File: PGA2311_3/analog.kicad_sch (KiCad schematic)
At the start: 88 parts, among them J201 3, J202 3, J203 2, J204 2, U201 OPA1678IDR, U202 CD74HCT4052, U203 CD74HCT4052, U204 LM337LM, U205 PGA2311UA, U206 LM317LIDR, U207 UA78L05AIDR

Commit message: Add files via upload
CS3 line added to connector
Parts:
- removed R229: 0, Resistor_SMD:R_0805_2012Metric_Pad1.20x1.40mm_HandSolder, symbol Device:R_Small
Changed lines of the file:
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@@
 		(title "Preamp2311")
 		(date "03.2026")
-		(rev "2")
+		(rev "2_1")
 		(company "DMSDL")
 		(comment 1 "designed by Oleg Voitovich")
@@
 	(wire
 		(pts
-			(xy 205.74 69.85) (xy 205.74 73.66)
-		)
-		(stroke
-			(width 0)
-			(type default)
-		)
-	)
-	(wire
-		(pts
 			(xy 204.47 54.61) (xy 205.74 54.61)
 		)
@@
 	(wire
 		(pts
-			(xy 205.74 69.85) (xy 208.28 69.85)
-		)
-		(stroke
-			(width 0)
-			(type default)
-		)
-	)
-	(wire
-		(pts
 			(xy 110.49 142.24) (xy 113.03 142.24)
 		)
@@
 	(wire
 		(pts
-			(xy 213.36 69.85) (xy 214.63 69.85)
-		)
-		(stroke
-			(width 0)
-			(type default)
-		)
-	)
-	(wire
-		(pts
 			(xy 142.24 180.34) (xy 142.24 181.61)
 		)
@@
 	(wire
 		(pts
-			(xy 214.63 69.85) (xy 214.63 73.66)
-		)
-		(stroke
-			(width 0)
-			(type default)
-		)
-	)
-	(wire
-		(pts
 			(xy 223.52 142.24) (xy 226.06 142.24)
 		)
@@
 	(symbol
 		(lib_id "power:GND")
-		(at 205.74 73.66 0)
-		(unit 1)
-		(exclude_from_sim no)
-		(in_bom yes)
-		(on_board yes)
-		(dnp no)
-		(property "Reference" "#PWR0249"
-			(at 205.74 80.01 0)
-			(effects
-				(font
-					(size 1.27 1.27)
-				)
-				(hide yes)
-			)
-		)
-		(property "Value" "GND"
-			(at 210.058 75.692 0)
-			(effects
-				(font
-					(size 1.27 1.27)
-				)
-			)
-		)
-		(property "Footprint" ""
-			(at 205.74 73.66 0)
-			(effects
-				(font
-					(size 1.27 1.27)
-				)
-				(hide yes)
-			)
-		)
-		(property "Datasheet" ""
-			(at 205.74 73.66 0)
-			(effects
-				(font
-					(size 1.27 1.27)
-				)
-				(hide yes)
-			)
-		)
-		(property "Description" "Power symbol creates a global label with name \"GND\" , ground"
-			(at 205.74 73.66 0)
-			(effects
-				(font
-					(size 1.27 1.27)
-				)
-				(hide yes)
-			)
-		)
-		(pin "1"
-		)
-		(instances
-			(project "PGA2311_3"
-				(path "/e4f5d1ca-8b46-4ca2-bb25-7f237c56d603/417e42a4-c07c-47f8-ba75-79030ad924cb"
-					(reference "#PWR0249")
-					(unit 1)
-				)
-			)
-		)
-	)
-	(symbol
-		(lib_id "power:GND")
 		(at 134.62 64.77 0)
 		(unit 1)
@@
 	)
 	(symbol
-		(lib_id "Device:R_Small")
-		(at 210.82 69.85 270)
-		(unit 1)
-		(exclude_from_sim no)
-		(in_bom yes)
-		(on_board yes)
-		(dnp no)
-		(property "Reference" "R229"
-			(at 214.63 66.802 90)
-			(effects
-				(font
-					(size 1.016 1.016)
-				)
-			)
-		)
-		(property "Value" "0"
-			(at 209.55 67.056 90)
-			(effects
-				(font
-					(size 1.27 1.27)
-				)
-			)
-		)
-		(property "Footprint" "Resistor_SMD:R_0805_2012Metric_Pad1.20x1.40mm_HandSolder"
-			(at 210.82 69.85 0)
-			(effects
-				(font
-					(size 1.27 1.27)
-				)
-				(hide yes)
-			)
-		)
-		(property "Datasheet" "~"
-			(at 210.82 69.85 0)
-			(effects
-				(font
-					(size 1.27 1.27)
-				)
-				(hide yes)
-			)
-		)
-		(property "Description" "Resistor, small symbol"
-			(at 210.82 69.85 0)
-			(effects
-				(font
-					(size 1.27 1.27)
-				)
-				(hide yes)
-			)
-		)
-		(pin "1"
-		)
-		(pin "2"
-		)
-		(instances
-			(project "PGA2311_3"
-				(path "/e4f5d1ca-8b46-4ca2-bb25-7f237c56d603/417e42a4-c07c-47f8-ba75-79030ad924cb"
-					(reference "R229")
-					(unit 1)
-				)
-			)
-		)
-	)
-	(symbol
 		(lib_id "power:GND")
 		(at 134.62 90.17 0)
@@
 					(unit 1)
 				)
-			)
-		)
-	)
-	(symbol
-		(lib_id "power:GND")
-		(at 214.63 73.66 0)
-		(unit 1)
-		(exclude_from_sim no)
-		(in_bom yes)
-		(on_board yes)
-		(dnp no)
-		(property "Reference" "#PWR0250"
-			(at 214.63 80.01 0)
-			(effects
-				(font
-					(size 1.27 1.27)
-				)
-				(hide yes)
-			)
-		)
-		(property "Value" "GND"
-			(at 218.948 75.692 0)
-			(effects
-				(font
-					(size 1.27 1.27)
-				)
-			)
-		)
-		(property "Footprint" ""
-			(at 214.63 73.66 0)
-			(effects
-				(font
-					(size 1.27 1.27)
-				)
-				(hide yes)
-			)
-		)
-		(property "Datasheet" ""
-			(at 214.63 73.66 0)
-			(effects
-				(font
-					(size 1.27 1.27)
-				)
-				(hide yes)
-			)
-		)
-		(property "Description" "Power symbol creates a global label with name \"GND\" , ground"
-			(at 214.63 73.66 0)
-			(effects
-				(font
-					(size 1.27 1.27)
-				)
-				(hide yes)
-			)
-		)
-		(pin "1"
-		)
-		(instances
-			(project "PGA2311_3"
-				(path "/e4f5d1ca-8b46-4ca2-bb25-7f237c56d603/417e42a4-c07c-47f8-ba75-79030ad924cb"
-					(reference "#PWR0250")
-					(unit 1)
-				)

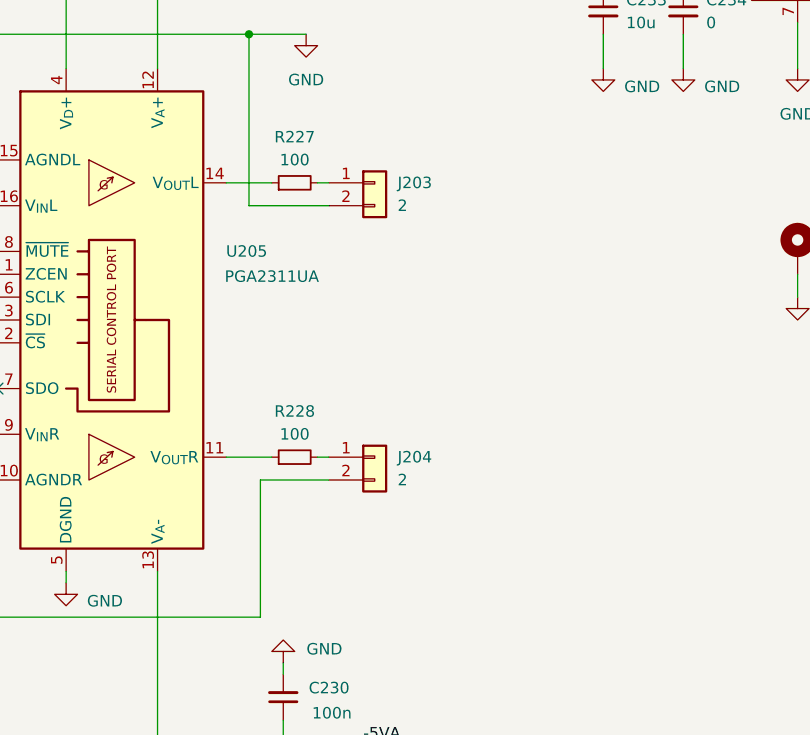
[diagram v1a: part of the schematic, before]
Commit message: Add files via upload
PGA output connector added
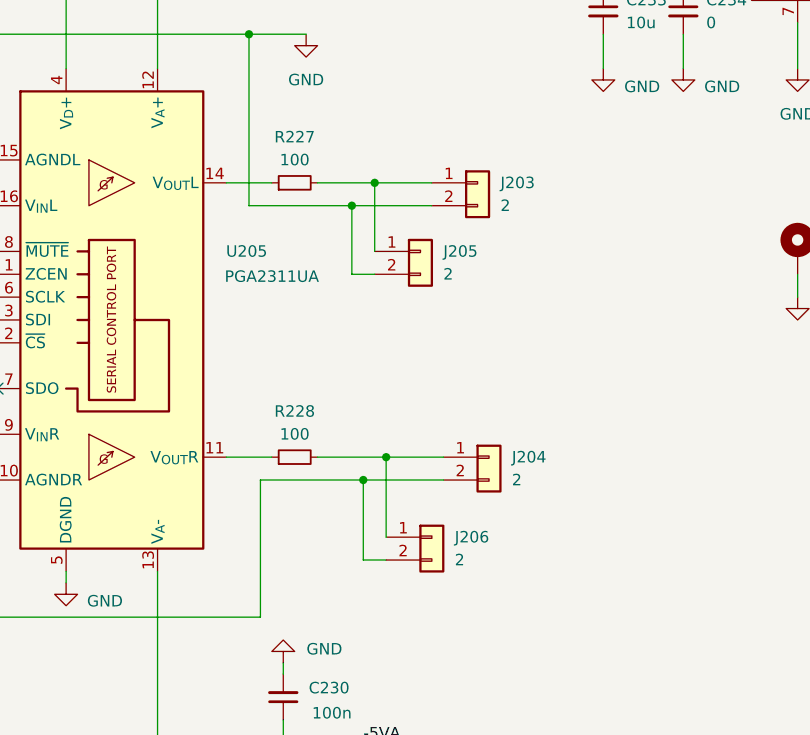
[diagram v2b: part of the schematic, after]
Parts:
- added J205, J206: 2, Connector_PinHeader_2.54mm:PinHeader_1x02_P2.54mm_Vertical, symbol Connector_Generic:Conn_01x02
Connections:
- net GND: now also J205.2 (Pin_2), J206.2 (Pin_2)
- net at J204.1 (Pin_1), R228.2: now also J206.1 (Pin_1)
- net at J203.1 (Pin_1), R227.2: now also J205.1 (Pin_1)
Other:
- moved on the sheet: J203, J204

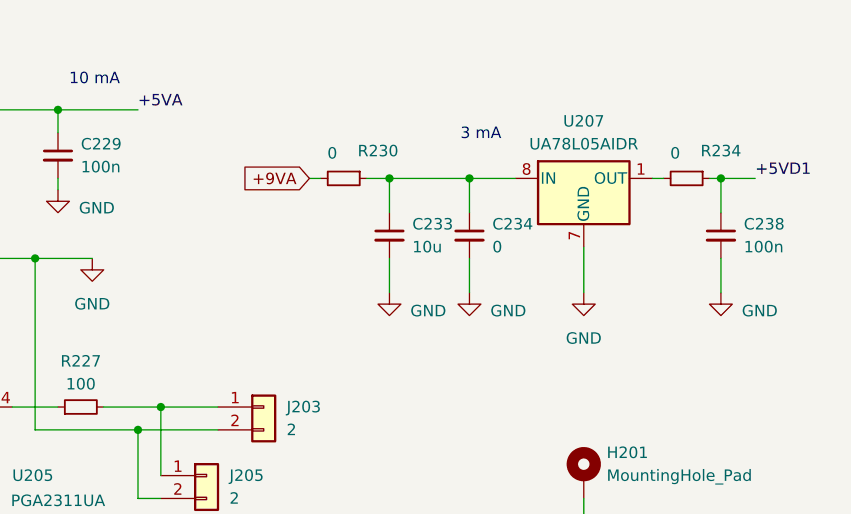
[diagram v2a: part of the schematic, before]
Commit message: Add files via upload
vias rearranged for connector placement
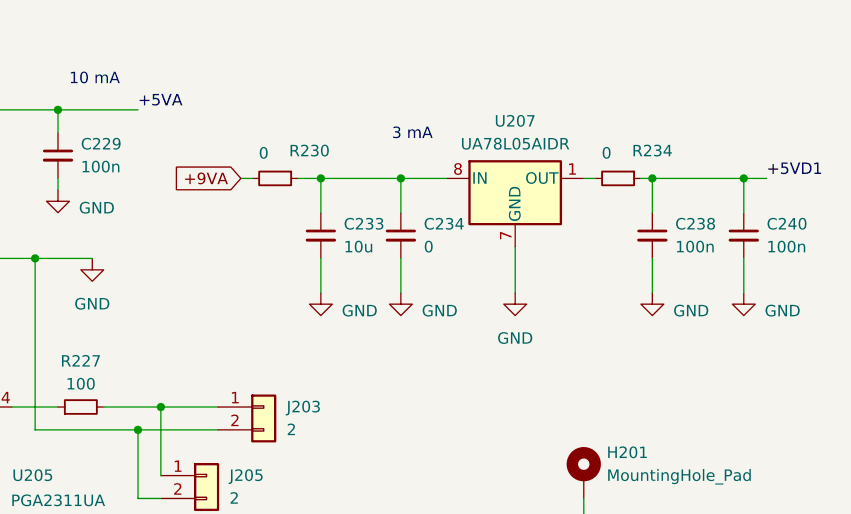
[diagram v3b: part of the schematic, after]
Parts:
- added C240: 100n, Capacitor_SMD:C_0805_2012Metric_Pad1.18x1.45mm_HandSolder, symbol Device:C_Small
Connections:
- net +5VD1: now also C240.1
- net GND: now also C240.2
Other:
- moved on the sheet: C233, C234, C238, R230, R234, U207

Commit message: Add files via upload
v.2.4 connector to +VA line added
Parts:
- added J207: 2, Connector_PinHeader_2.54mm:PinHeader_1x02_P2.54mm_Vertical, symbol Connector_Generic:Conn_01x02
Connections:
- net +9VA: now also J207.2 (Pin_2)
- net GND: now also J207.1 (Pin_1)
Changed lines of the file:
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@@
 		(title "Preamp2311")
 		(date "03.2026")
-		(rev "2_3")
+		(rev "2_4")
 		(company "DMSDL")
 		(comment 1 "designed by Oleg Voitovich")
@@
 	)
 	(junction
+		(at 180.34 142.24)
+		(diameter 0)
+		(color 0 0 0 0)
+	)
+	(junction
 		(at 132.08 172.72)
 		(diameter 0)
@@
 	(wire
 		(pts
-			(xy 184.15 142.24) (xy 185.42 142.24)
+			(xy 173.99 142.24) (xy 180.34 142.24)
 		)
 		(stroke
@@
 	(wire
 		(pts
+			(xy 180.34 142.24) (xy 185.42 142.24)
+		)
+		(stroke
+			(width 0)
+			(type default)
+		)
+	)
+	(wire
+		(pts
 			(xy 172.72 16.51) (xy 190.5 16.51)
 		)
@@
 	(wire
 		(pts
+			(xy 181.61 133.35) (xy 180.34 133.35)
+		)
+		(stroke
+			(width 0)
+			(type default)
+		)
+	)
+	(wire
+		(pts
 			(xy 26.67 58.42) (xy 26.67 66.04)
 		)
@@
 	(wire
 		(pts
+			(xy 173.99 130.81) (xy 181.61 130.81)
+		)
+		(stroke
+			(width 0)
+			(type default)
+		)
+	)
+	(wire
+		(pts
 			(xy 97.79 66.04) (xy 96.52 66.04)
 		)
@@
 	(wire
 		(pts
+			(xy 173.99 130.81) (xy 173.99 134.62)
+		)
+		(stroke
+			(width 0)
+			(type default)
+		)
+	)
+	(wire
+		(pts
 			(xy 30.48 39.37) (xy 30.48 43.18)
 		)
@@
 	(wire
 		(pts
+			(xy 180.34 133.35) (xy 180.34 142.24)
+		)
+		(stroke
+			(width 0)
+			(type default)
+		)
+	)
+	(wire
+		(pts
 			(xy 124.46 81.28) (xy 124.46 72.39)
 		)
@@
 	(global_label "+9VA"
 		(shape input)
-		(at 184.15 142.24 180)
+		(at 173.99 142.24 180)
 		(fields_autoplaced yes)
 		(effects
@@
 		)
 		(property "Intersheetrefs" "${INTERSHEET_REFS}"
-			(at 176.2057 142.24 0)
+			(at 166.0457 142.24 0)
 			(effects
 				(font
@@
 	(symbol
 		(lib_id "power:GND")
+		(at 173.99 134.62 0)
+		(unit 1)
+		(exclude_from_sim no)
+		(in_bom yes)
+		(on_board yes)
+		(dnp no)
+		(property "Reference" "#PWR0250"
+			(at 173.99 140.97 0)
+			(effects
+				(font
+					(size 1.27 1.27)
+				)
+				(hide yes)
+			)
+		)
+		(property "Value" "GND"
+			(at 178.308 136.652 0)
+			(effects
+				(font
+					(size 1.27 1.27)
+				)
+			)
+		)
+		(property "Footprint" ""
+			(at 173.99 134.62 0)
+			(effects
+				(font
+					(size 1.27 1.27)
+				)
+				(hide yes)
+			)
+		)
+		(property "Datasheet" ""
+			(at 173.99 134.62 0)
+			(effects
+				(font
+					(size 1.27 1.27)
+				)
+				(hide yes)
+			)
+		)
+		(property "Description" "Power symbol creates a global label with name \"GND\" , ground"
+			(at 173.99 134.62 0)
+			(effects
+				(font
+					(size 1.27 1.27)
+				)
+				(hide yes)
+			)
+		)
+		(pin "1"
+		)
+		(instances
+			(project "PGA2311_3"
+				(path "/e4f5d1ca-8b46-4ca2-bb25-7f237c56d603/417e42a4-c07c-47f8-ba75-79030ad924cb"
+					(reference "#PWR0250")
+					(unit 1)
+				)
+			)
+		)
+	)
+	(symbol
+		(lib_id "power:GND")
 		(at 203.2 38.1 0)
 		(unit 1)
@@
 					(unit 1)
 				)
+			)
+		)
+	)
+	(symbol
+		(lib_id "Connector_Generic:Conn_01x02")
+		(at 186.69 130.81 0)
+		(unit 1)
+		(exclude_from_sim no)
+		(in_bom yes)
+		(on_board yes)
+		(dnp no)
+		(fields_autoplaced yes)
+		(property "Reference" "J207"
+			(at 189.23 130.8099 0)
+			(effects
+				(font
+					(size 1.27 1.27)
+				)
+				(justify left)
+			)
+		)
+		(property "Value" "2"
+			(at 189.23 133.3499 0)
+			(effects
+				(font
+					(size 1.27 1.27)
+				)
+				(justify left)
+			)
+		)
+		(property "Footprint" "Connector_PinHeader_2.54mm:PinHeader_1x02_P2.54mm_Vertical"
+			(at 186.69 130.81 0)
+			(effects
+				(font
+					(size 1.27 1.27)
+				)
+				(hide yes)
+			)
+		)
+		(property "Datasheet" "~"
+			(at 186.69 130.81 0)
+			(effects
+				(font
+					(size 1.27 1.27)
+				)
+				(hide yes)
+			)
+		)
+		(property "Description" "Generic connector, single row, 01x02, script generated (kicad-library-utils/schlib/autogen/connector/)"
+			(at 186.69 130.81 0)
+			(effects
+				(font
+					(size 1.27 1.27)
+				)
+				(hide yes)
+			)
+		)
+		(pin "1"
+		)
+		(pin "2"
+		)
+		(instances
+			(project "PGA2311_3"
+				(path "/e4f5d1ca-8b46-4ca2-bb25-7f237c56d603/417e42a4-c07c-47f8-ba75-79030ad924cb"
+					(reference "J207")
+					(unit 1)
+				)

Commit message: Add files via upload
78l05 output R0 removed
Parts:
- removed R234: 0, Resistor_SMD:R_0805_2012Metric_Pad1.20x1.40mm_HandSolder, symbol Device:R_Small
- R205, R206: value 10 -> 100
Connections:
- net +5VD1: now also U207.1 (OUT)
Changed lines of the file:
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@@
 	(wire
 		(pts
-			(xy 257.81 29.21) (xy 259.08 29.21)
+			(xy 257.81 29.21) (xy 265.43 29.21)
 		)
 		(stroke
@@
 	(wire
 		(pts
-			(xy 264.16 29.21) (xy 265.43 29.21)
-		)
-		(stroke
-			(width 0)
-			(type default)
-		)
-	)
-	(wire
-		(pts
 			(xy 163.83 64.77) (xy 163.83 34.29)
 		)
@@
 			)
 		)
-		(property "Value" "10"
+		(property "Value" "100"
 			(at 77.216 93.98 90)
 			(effects
@@
 			)
 		)
-		(property "Value" "10"
+		(property "Value" "100"
 			(at 74.676 15.24 90)
 			(effects
@@
 					(unit 1)
 				)
-			)
-		)
-	)
-	(symbol
-		(lib_id "Device:R_Small")
-		(at 261.62 29.21 270)
-		(unit 1)
-		(exclude_from_sim no)
-		(in_bom yes)
-		(on_board yes)
-		(dnp no)
-		(property "Reference" "R234"
-			(at 265.43 26.162 90)
-			(effects
-				(font
-					(size 1.27 1.27)
-				)
-			)
-		)
-		(property "Value" "0"
-			(at 260.35 26.416 90)
-			(effects
-				(font
-					(size 1.27 1.27)
-				)
-			)
-		)
-		(property "Footprint" "Resistor_SMD:R_0805_2012Metric_Pad1.20x1.40mm_HandSolder"
-			(at 261.62 29.21 0)
-			(effects
-				(font
-					(size 1.27 1.27)
-				)
-				(hide yes)
-			)
-		)
-		(property "Datasheet" "~"
-			(at 261.62 29.21 0)
-			(effects
-				(font
-					(size 1.27 1.27)
-				)
-				(hide yes)
-			)
-		)
-		(property "Description" "Resistor, small symbol"
-			(at 261.62 29.21 0)
-			(effects
-				(font
-					(size 1.27 1.27)
-				)
-				(hide yes)
-			)
-		)
-		(pin "1"
-		)
-		(pin "2"
-		)
-		(instances
-			(project "PGA2311_3"
-				(path "/e4f5d1ca-8b46-4ca2-bb25-7f237c56d603/417e42a4-c07c-47f8-ba75-79030ad924cb"
-					(reference "R234")
-					(unit 1)
-				)

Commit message: Add files via upload
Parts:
- C240: value 100n -> 10u
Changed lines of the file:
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@@
 			)
 		)
-		(property "Value" "100n"
+		(property "Value" "10u"
 			(at 278.13 36.8362 0)
 			(effects

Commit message: Add files via upload
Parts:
- added J208: 2, Connector_PinHeader_2.54mm:PinHeader_1x02_P2.54mm_Vertical, symbol Connector_Generic:Conn_01x02
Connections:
- net -9VA: now also J208.2 (Pin_2)
- net GND: now also J208.1 (Pin_1)
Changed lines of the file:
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@@
 	(wire
 		(pts
-			(xy 76.2 172.72) (xy 77.47 172.72)
+			(xy 71.12 172.72) (xy 77.47 172.72)
 		)
 		(stroke
@@
 	(wire
 		(pts
+			(xy 77.47 161.29) (xy 71.12 161.29)
+		)
+		(stroke
+			(width 0)
+			(type default)
+		)
+	)
+	(wire
+		(pts
 			(xy 161.29 34.29) (xy 161.29 62.23)
 		)
@@
 	(wire
 		(pts
+			(xy 71.12 161.29) (xy 71.12 166.37)
+		)
+		(stroke
+			(width 0)
+			(type default)
+		)
+	)
+	(wire
+		(pts
 			(xy 64.77 63.5) (xy 64.77 43.18)
 		)
@@
 	(wire
 		(pts
+			(xy 77.47 163.83) (xy 77.47 172.72)
+		)
+		(stroke
+			(width 0)
+			(type default)
+		)
+	)
+	(wire
+		(pts
 			(xy 162.56 172.72) (xy 162.56 175.26)
 		)
@@
 	(global_label "-9VA"
 		(shape input)
-		(at 76.2 172.72 180)
+		(at 71.12 172.72 180)
 		(fields_autoplaced yes)
 		(effects
@@
 		)
 		(property "Intersheetrefs" "${INTERSHEET_REFS}"
-			(at 68.2557 172.72 0)
+			(at 63.1757 172.72 0)
 			(effects
 				(font
@@
 	)
 	(symbol
+		(lib_id "Connector_Generic:Conn_01x02")
+		(at 82.55 161.29 0)
+		(unit 1)
+		(exclude_from_sim no)
+		(in_bom yes)
+		(on_board yes)
+		(dnp no)
+		(fields_autoplaced yes)
+		(property "Reference" "J208"
+			(at 85.09 161.2899 0)
+			(effects
+				(font
+					(size 1.27 1.27)
+				)
+				(justify left)
+			)
+		)
+		(property "Value" "2"
+			(at 85.09 163.8299 0)
+			(effects
+				(font
+					(size 1.27 1.27)
+				)
+				(justify left)
+			)
+		)
+		(property "Footprint" "Connector_PinHeader_2.54mm:PinHeader_1x02_P2.54mm_Vertical"
+			(at 82.55 161.29 0)
+			(effects
+				(font
+					(size 1.27 1.27)
+				)
+				(hide yes)
+			)
+		)
+		(property "Datasheet" "~"
+			(at 82.55 161.29 0)
+			(effects
+				(font
+					(size 1.27 1.27)
+				)
+				(hide yes)
+			)
+		)
+		(property "Description" "Generic connector, single row, 01x02, script generated (kicad-library-utils/schlib/autogen/connector/)"
+			(at 82.55 161.29 0)
+			(effects
+				(font
+					(size 1.27 1.27)
+				)
+				(hide yes)
+			)
+		)
+		(pin "1"
+		)
+		(pin "2"
+		)
+		(instances
+			(project "PGA2311_3"
+				(path "/e4f5d1ca-8b46-4ca2-bb25-7f237c56d603/417e42a4-c07c-47f8-ba75-79030ad924cb"
+					(reference "J208")
+					(unit 1)
+				)
+			)
+		)
+	)
+	(symbol
 		(lib_id "Device:C_Small")
 		(at 36.83 66.04 90)
@@
 					(unit 1)
 				)
+			)
+		)
+	)
+	(symbol
+		(lib_id "power:GND")
+		(at 71.12 166.37 0)
+		(unit 1)
+		(exclude_from_sim no)
+		(in_bom yes)
+		(on_board yes)
+		(dnp no)
+		(property "Reference" "#PWR0262"
+			(at 71.12 172.72 0)
+			(effects
+				(font
+					(size 1.27 1.27)
+				)
+				(hide yes)
+			)
+		)
+		(property "Value" "GND"
+			(at 75.438 168.402 0)
+			(effects
+				(font
+					(size 1.27 1.27)
+				)
+			)
+		)
+		(property "Footprint" ""
+			(at 71.12 166.37 0)
+			(effects
+				(font
+					(size 1.27 1.27)
+				)
+				(hide yes)
+			)
+		)
+		(property "Datasheet" ""
+			(at 71.12 166.37 0)
+			(effects
+				(font
+					(size 1.27 1.27)
+				)
+				(hide yes)
+			)
+		)
+		(property "Description" "Power symbol creates a global label with name \"GND\" , ground"
+			(at 71.12 166.37 0)
+			(effects
+				(font
+					(size 1.27 1.27)
+				)
+				(hide yes)
+			)
+		)
+		(pin "1"
+		)
+		(instances
+			(project "PGA2311_3"
+				(path "/e4f5d1ca-8b46-4ca2-bb25-7f237c56d603/417e42a4-c07c-47f8-ba75-79030ad924cb"
+					(reference "#PWR0262")
+					(unit 1)
+				)
